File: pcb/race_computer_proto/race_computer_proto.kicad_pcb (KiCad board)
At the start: 4 copper layers, 200.7 x 125.7 mm, 19 parts, among them U1 Teensy4.0, U3 SN74LVC245APW

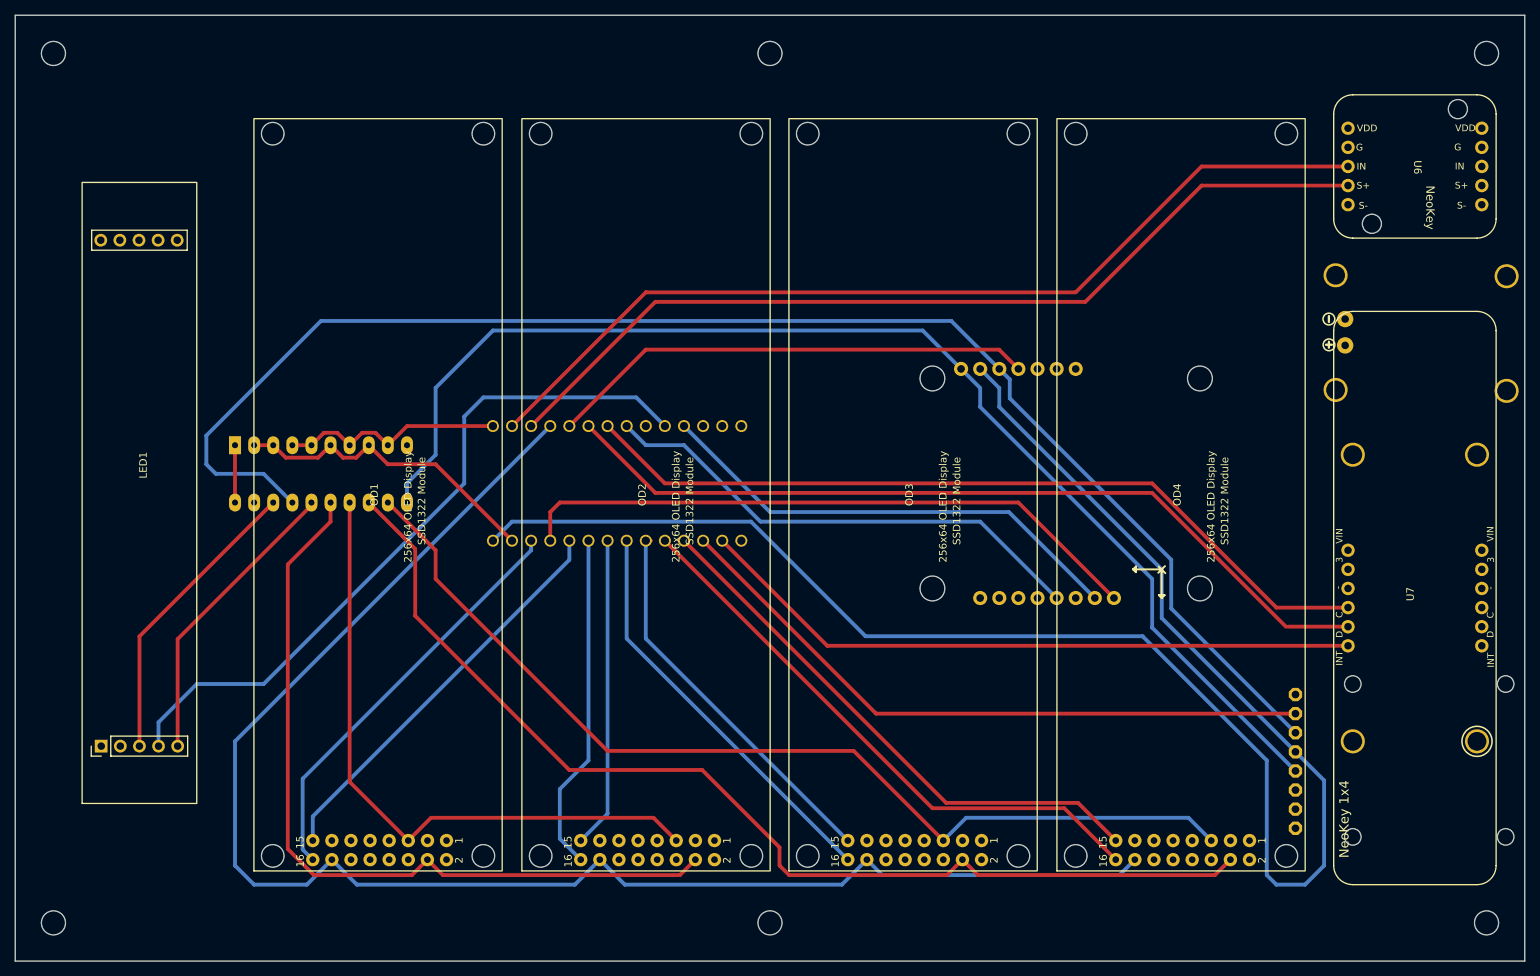
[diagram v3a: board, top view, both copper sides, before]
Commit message: PCB redesign.  OLEDs and other secondary modules moved off board and replaced with headers for cable connections. Only Teensy and GPS modules remain on primary board.
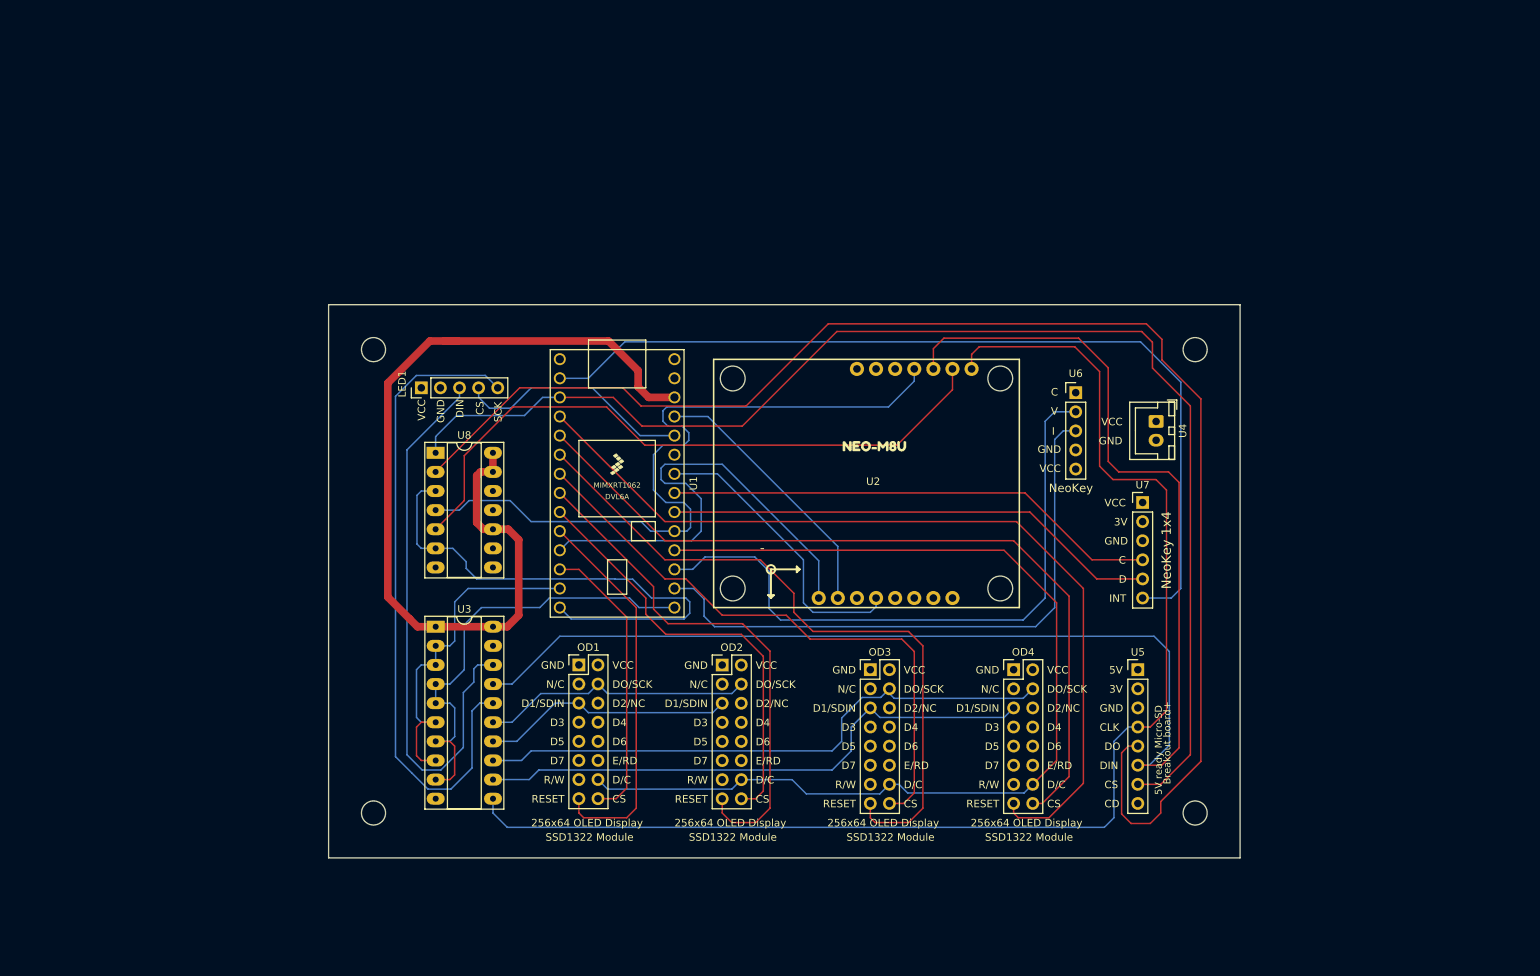
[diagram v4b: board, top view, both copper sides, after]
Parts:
- removed the REF** at (149.9, 35.6)
- removed the REF** at (149.9, 151.1)
- added U8: 74LS125, Package_DIP:DIP-14_W7.62mm_Socket_LongPads, F.Cu at (105.4, 88.6)
- LED1: footprint race_computer:8-Digit 7 Segment MAX7219 Module -> race_computer:7seg_max7219_module_header
- OD1, OD2, OD3, OD4: footprint race_computer:OLED_Display -> race_computer:OLED_header
- U1, U2, U3: moved to F.Cu
- U4: footprint race_computer:AdaFruit_USB_C_PD -> race_computer:power_header; moved to F.Cu
- U5: footprint race_computer:AdaFruit_MicroSD+ -> race_computer:microsd_breakout_header; moved to F.Cu
- U6: footprint race_computer:neokey_MX_breakout -> race_computer:neokey_header
- U7: footprint race_computer:NeoKey1x4 -> race_computer:neokey_1x4_header
- moved REF** 98.4 mm to (162.9, 96.4), turned to 180 degrees
- moved LED1 63.9 mm to (103.5, 80.0)
- moved REF** 58.0 mm to (97.2, 74.9)
- moved REF** 55.2 mm to (206.4, 74.9)
- moved U6 54.0 mm to (190.5, 80.7), turned to 0 degrees
- moved REF** 45.0 mm to (97.2, 136.5)
- moved REF** 41.4 mm to (206.4, 136.5)
- moved U7 38.1 mm to (199.4, 95.2), turned to 0 degrees
- moved U4 37.1 mm to (201.2, 84.5), turned to -90 degrees
- moved U5 37.0 mm to (198.8, 117.5), turned to 0 degrees
- moved U3 36.0 mm to (105.4, 111.8), turned to 0 degrees
- moved OD1 35.0 mm to (124.5, 116.8), turned to 0 degrees
- moved OD4 32.2 mm to (182.2, 117.5), turned to 0 degrees
- moved OD2 24.8 mm to (143.5, 116.9), turned to 0 degrees
- moved U2 24.8 mm to (163.6, 93.0), turned to 0 degrees
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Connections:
- U2 pad 10: /MISO -> Net-(U2-TX/MISO)
- U5 pad 5: /MISO -> Net-(U5-DO)
- U6 pad 2: GND -> Net-(U1-15_A1_RX3_SPDIF_IN)
- U6 pad 4: Net-(U1-15_A1_RX3_SPDIF_IN) -> GND
- U6 pad 5: unconnected-(U6-S--Pad5) -> +5V
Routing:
- net Net-(U5-DO): track 0.00 -> 191.8 mm
- net /MISO: track 226.5 -> 68.9 mm
- net Net-(U2-TX/MISO): track 0.00 -> 86.9 mm
- net /SDCARD_CS: track 88.3 -> 172.5 mm
- net /DISP_BUS.SCK0: track 106.6 -> 36.2 mm
- net /DISP_BUS.SCK1: track 144.2 -> 78.9 mm
- net /DISP_BUS.DC: track 205.0 -> 140.2 mm
- net /DISP_BUS.CS4: track 95.2 -> 31.6 mm
- net /DISP_BUS.MOSI1: track 132.8 -> 76.1 mm
- net /DISP_BUS.MOSI0: track 86.3 -> 33.6 mm
- net /3V3: track 74.5 -> 122.4 mm
- net /DISP_BUS.SCK2: track 39.7 -> 87.3 mm
- net /SDA: track 111.7 -> 65.9 mm
- net Net-(U1-14_A0_TX3_SPDIF_OUT): track 125.4 -> 80.7 mm
- net /DISP_BUS.RESET3: track 73.9 -> 117.7 mm
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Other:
- board size 200.7 x 125.7 mm -> 121.2 x 73.5 mm
- board text added: "Rev ${REVISION}"

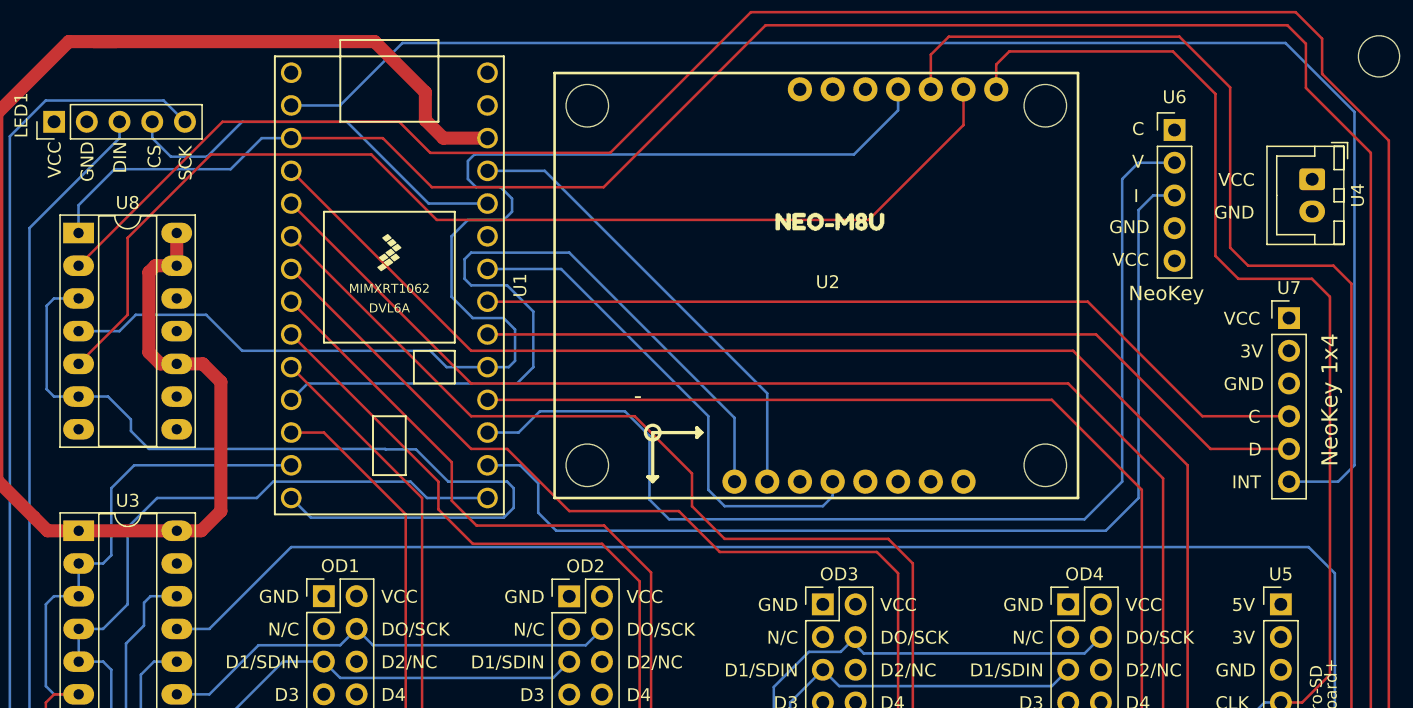
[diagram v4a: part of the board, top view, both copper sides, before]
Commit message: Minor routing changes to remove some snaked traces.
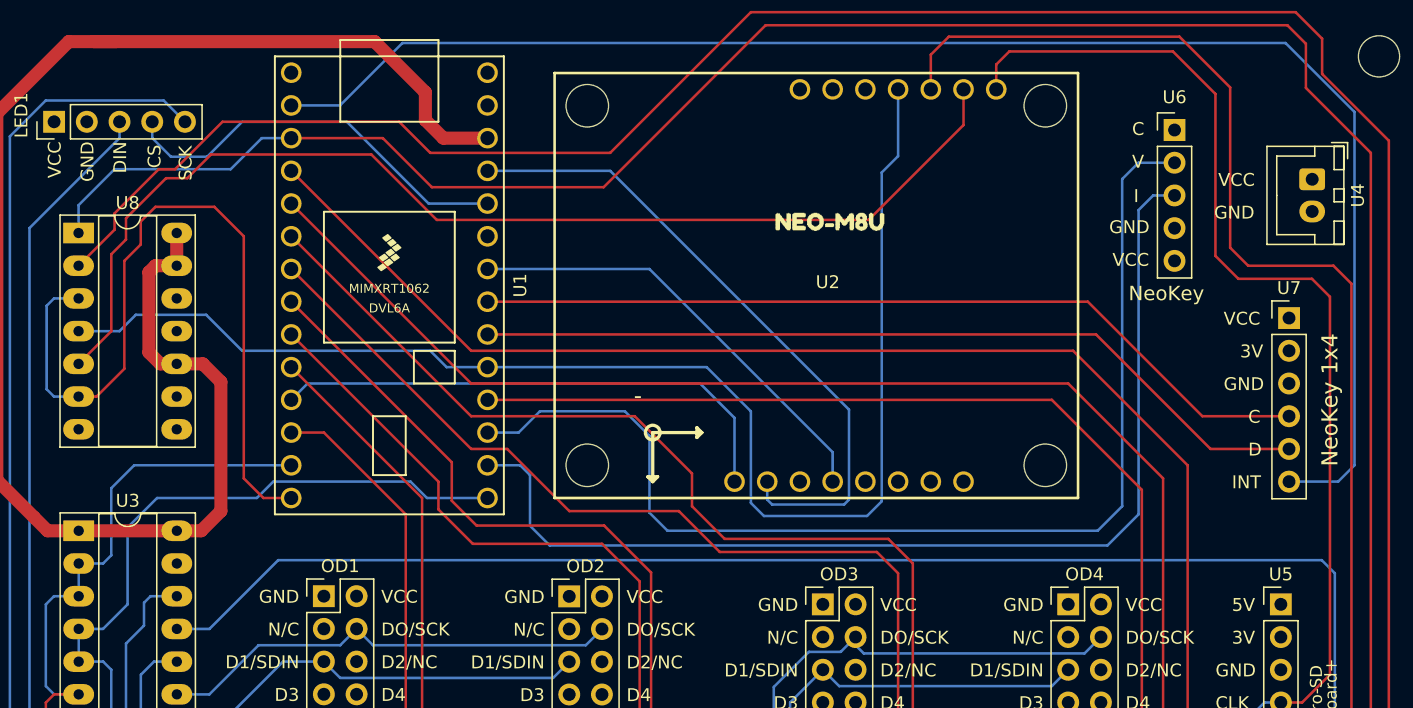
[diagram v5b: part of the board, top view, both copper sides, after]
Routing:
- net Net-(U1-9_OUT1C): track 63.5 -> 41.0 mm
- net /GPS_RST: track 35.7 -> 50.8 mm
- net Net-(U1-17_A3_TX4_SDA1): track 98.0 -> 106.5 mm
- net /MISO: track 68.9 -> 60.8 mm
- net /GPS_INT: track 39.2 -> 35.0 mm
- net Net-(U1-14_A0_TX3_SPDIF_OUT): track 80.7 -> 83.3 mm
- net Net-(U1-15_A1_RX3_SPDIF_IN): track 85.6 -> 88.1 mm
- net Net-(U2-TX/MISO): track 86.9 -> 87.8 mm
- net /GPS_SD_MOSI: track 204.0 -> 203.2 mm
- net Net-(U5-DO): track 191.8 -> 192.6 mm

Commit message: Updated case for the new PCB.  Includes models for electronics. Minor PCB fix -- GND connection was missing from the NeoKey connector, so the button would not register when pushed.
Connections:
- U6 pad 1: unconnected-(U6-S--Pad1) -> GND
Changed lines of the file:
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@@
 	(net 74 "Net-(U1-14_A0_TX3_SPDIF_OUT)")
 	(net 75 "Net-(U1-9_OUT1C)")
-	(net 76 "unconnected-(U6-S--Pad1)")
 	(footprint "race_computer:power_header"
 		(layer "F.Cu")
@@
 			)
 		)
-		(fp_text user "V"
+		(fp_text user "A"
 			(at -2.413 3.175 0)
 			(unlocked yes)
@@
 			)
 		)
-		(fp_text user "V"
+		(fp_text user "A"
 			(at -3.302 3.048 0)
 			(unlocked yes)
@@
 			)
 			(remove_unused_layers no)
-			(net 76 "unconnected-(U6-S--Pad1)")
+			(net 5 "GND")
 			(pinfunction "S-")
 			(pintype "output")
